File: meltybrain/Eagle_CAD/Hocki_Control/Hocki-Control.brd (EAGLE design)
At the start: 90 x 46 mm, 153 parts, among them J1 SM03B-SRSS-TB(LF)(SN), J2 SM04B-SRSS-TB(LF)(SN), J3 SM02B-SRSS-TB(LF)(SN), J4 SM04B-SRSS-TB(LF)(SN), J5 SM03B-SRSS-TB(LF)(SN), J6 SM03B-SRSS-TB(LF)(SN), U1 AP63200, U10 LMH6612MAX/NOPB, U11 TLV3502AIDCNR, U12 LMH6612MAX/NOPB, U13 TMP235A4DCKR, U14 ADXL375, U15 NL27WZ32USG, U16 ADXL375, U17 ADXL375, U18 NL27WZ32USG, U19 ADXL375, U2 TEENSY_4.1, U20 LMV358, U21 LMV358, U22 HMC1052L-TR, U23 LMV358, U24 IRF7509, U3 AP2210K-5.0TRG1, U4 AP2210K-3.3TRG1, U5 HEF4104BT,653, U6 LDL212PU50R, U7 LMH6612MAX/NOPB, U8 LMH6612MAX/NOPB, U9 TMUX1219DCKR

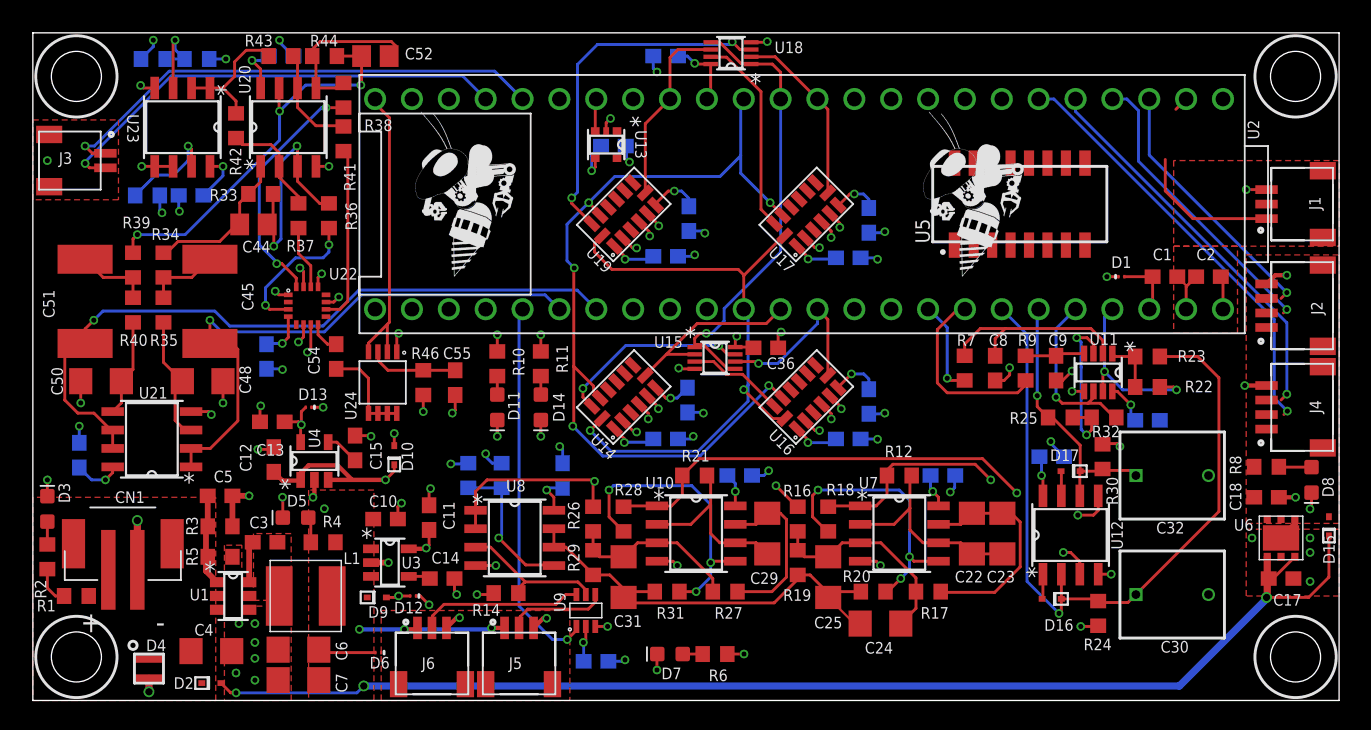
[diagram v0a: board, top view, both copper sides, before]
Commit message: fixed magnetometer issues
using instrumentation amplifier without filtering...fixes positive feedback as well
added ferrite bead
replaced remaining lmv358 to condense component list
TODO: esc connections
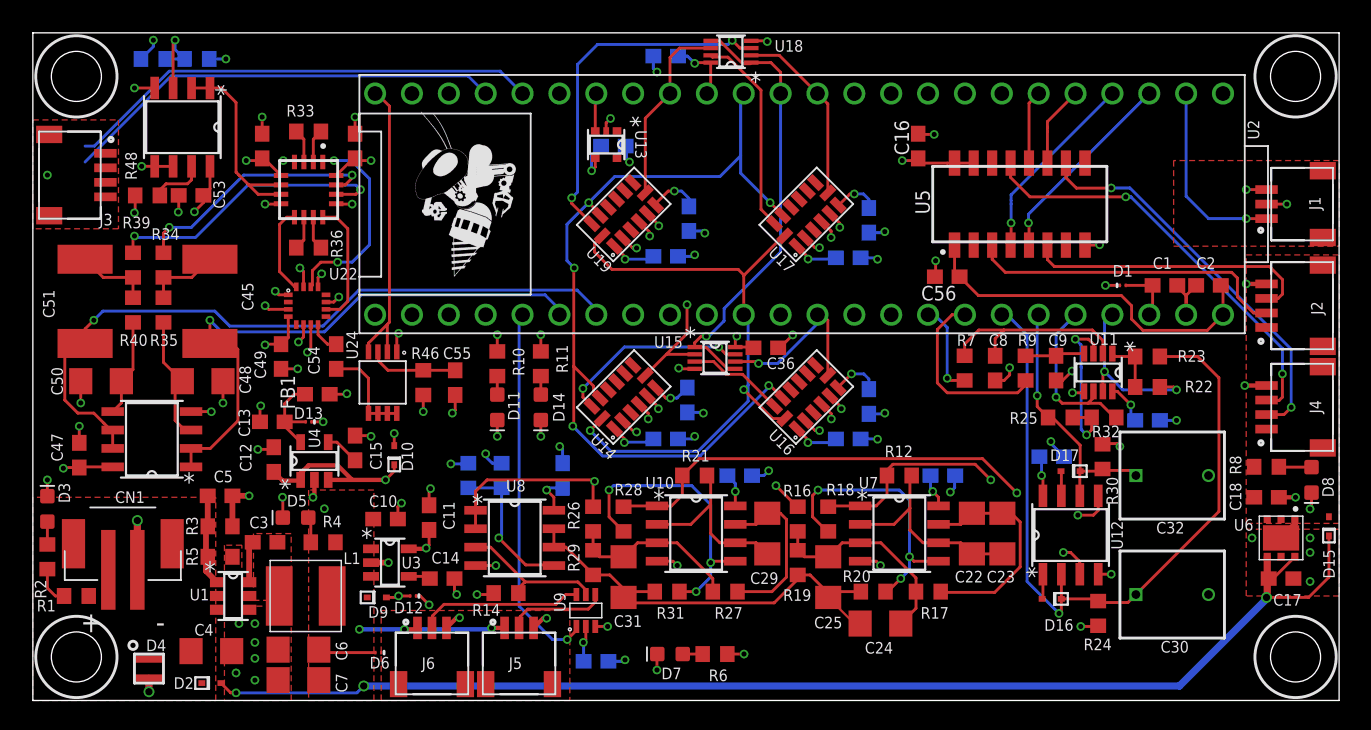
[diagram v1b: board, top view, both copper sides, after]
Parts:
- removed C52: 1000pF, rcl:C0805
- removed R37, R38, R41: 4.99k, rcl:R0603
- removed R42, R43, R44: 499k, rcl:R0603
- removed U$1: (no value), RoboJackets-Aesthetics:ROBOBUZZ_0.6X
- added C16, C56: 0.1uF, rcl:C0603
- added FB1: MPZ1608R391ATD25, Hocki_Library:0603
- C44: value 1000pF -> 0.1uF; device rcl:C0805 -> rcl:C0603
- CN1: value (none) -> JST_2PIN
- J3: value SM02B-SRSS-TB(LF)(SN) -> SM04B-SRSS-TB(LF)(SN); device Hocki_Library:SM02B-SRSS-TB(LF)(SN) -> Hocki_Library:SM04B-SRSS-TB(LF)(SN)
- R33: value 499k -> 49.9
- R36: value 4.99k -> 49.9
- U20: value LMV358 -> AD8426ACPZ-WP; device Hocki_Library:8-SOIC -> Hocki_Library:16LFCSP
- U21, U23: value LMV358 -> LMH6612MAX/NOPB
- moved C46 8.03 mm to (-29.8, 11.0), flipped to the top, turned to 90 degrees
- moved C44 5.43 mm to (-36.2, 11.0), turned to 90 degrees
- moved R33 5.42 mm to (-33.0, 12.0), turned to 180 degrees
- moved U20 4.52 mm to (-33.0, 8.00), turned to 270 degrees
- moved R36 2.61 mm to (-33.0, 4.00), turned to 180 degrees
- moved C49 1.00 mm to (-34.9, -3.50), flipped to the top
- moved D13 1.00 mm to (-33.0, -8.00)
- moved J3 1.00 mm to (-47.0, 9.00)
- moved D1 0.61 mm to (23.1, 1.40)
- moved C1 0.60 mm to (26.0, 1.40)
- moved C2 0.60 mm to (29.0, 1.40)
- moved U18 0.10 mm to (-3.90, 17.5)
- flipped C47 to the top
- flipped C53 to the top, turned to 180 degrees
- flipped R48 to the top
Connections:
- removed net MAG_OUTPUTA: C44.2, R33.1, R34.2, U20.1
- removed net MAG_OUTPUTB: C52.2, R39.2, R44.1, U20.7
- removed net OUT+(A): R36.2, U22.3
- removed net OUT+(B): R38.2, U22.16
- removed net OUT-(A): R37.2, U22.14
- removed net OUT-(B): R41.2, U22.10
- new net N$28: C13.1, D13.C2, FB1.1, U4.5
- new net N$31: U20.4, U22.3
- new net N$32: U20.1, U22.14
- new net N$33: U20.9, U22.16
- new net N$38: R33.1, U20.2
- new net N$39: R36.2, U20.10
- new net N$40: R36.1, U20.11
- net +3V3: now also C44.1, FB1.2, U20.16, U20.5; no longer C13.1, D13.C2, U20.8, U4.5
- net +5V: no longer U5.1
- net 3.3V: now also C16.1
- net 5V: now also C56.1, U5.1
- net ESC_L: no longer J3.1
- net ESC_R: no longer J3.2
- net GND: now also C16.2, C44.2, C56.2, U20.13, U20.8; no longer U20.4
- net LED_CLK2: now also U2.3; no longer U2.4
- net LED_DATA2: now also U2.4; no longer U2.3
- net N$34: now also U20.12, U22.10; no longer R41.1, R43.1, U20.6
- net N$35: now also R39.2, U20.14; no longer C52.1, R38.1, R44.2, U20.5
- net N$36: now also R34.2, U20.15; no longer R37.1, R42.1, U20.2
- net N$37: no longer C44.1, R36.1
- net VREF/2: now also U20.6, U20.7; no longer R42.2, R43.2
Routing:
- net B_LED_DATA2: track 0.00 -> 29.2 mm, vias 0 -> 2
- net MAG_OUTPUTB: track 27.5 -> 0.00 mm, vias 3 -> 0
- net B_LED_CLK2: track 0.00 -> 27.3 mm, vias 0 -> 2
- net LED_CLK2: track 29.6 -> 5.60 mm, vias 1 -> 0
- net 5V: track 30.9 -> 53.6 mm
- net 3.3V: track 47.1 -> 69.4 mm, vias 14 -> 16
- net B_LED_CLK1: track 0.00 -> 22.2 mm
- net LED_DATA2: track 26.9 -> 5.07 mm, vias 1 -> 0
- net B_LED_DATA1: track 0.00 -> 20.0 mm
- net OUT+(B): track 16.9 -> 0.00 mm, vias 2 -> 0
- net N$37: track 16.8 -> 2.32 mm, vias 2 -> 0
- net N$32: track 0.00 -> 14.2 mm, vias 0 -> 2
- net N$31: track 0.00 -> 13.0 mm, vias 0 -> 2
- net OUT-(B): track 12.2 -> 0.00 mm
- net MAG_OUTPUTA: track 10.7 -> 0.00 mm
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- added copper zone on layer 1, net 3.3V
- removed copper zone on layer 1, net 5V

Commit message: finished esc connections...moved connector a bit as well
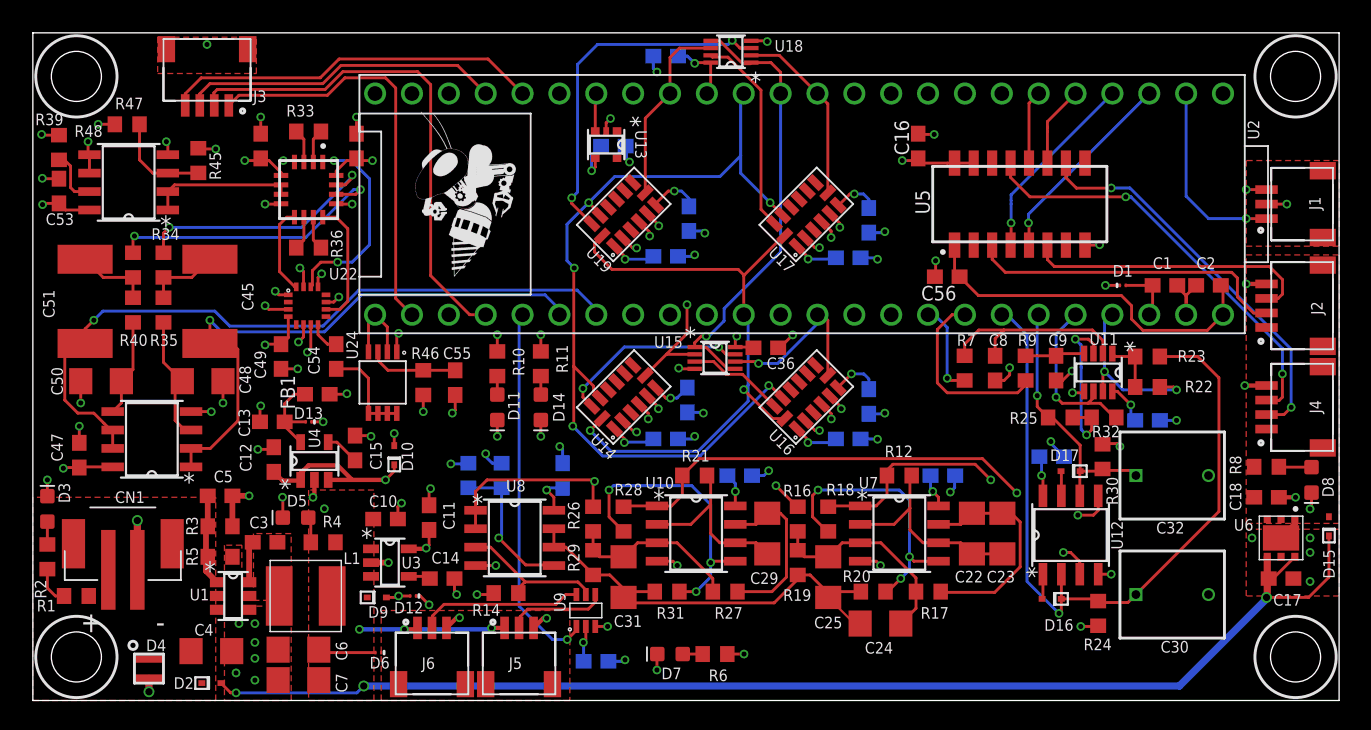
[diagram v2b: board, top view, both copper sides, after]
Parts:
- moved C53 9.10 mm to (-50.2, 7.90), turned to 90 degrees
- moved J3 8.49 mm to (-40.0, 13.8), turned to 180 degrees
- moved R45 7.00 mm to (-40.6, 10.0), flipped to the top, turned to 270 degrees
- moved R48 6.94 mm to (-50.2, 10.9), turned to 90 degrees
- moved U23 5.30 mm to (-45.4, 8.50), turned to 180 degrees
- moved R47 4.85 mm to (-45.5, 12.5), flipped to the top, turned to 180 degrees
- moved C46 0.10 mm to (-29.7, 11.0)
- moved C44 0.10 mm to (-36.3, 11.0)
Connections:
- new net ESC_TEL_L: J3.4, U2.28
- new net ESC_TEL_R: J3.1, U2.34
- net ESC_L: now also J3.3, U2.29; no longer U2.28
- net ESC_R: now also J3.2, U2.36; no longer U2.29
- net S/R: now also U2.33; no longer U2.32
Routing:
- net ESC_TEL_R: track 0.00 -> 28.7 mm
- net ESC_TEL_L: track 0.00 -> 26.0 mm
- net S/R: track 20.8 -> 5.66 mm
- net ESC_L: track 32.9 -> 22.1 mm
- net VREF/2: track 14.2 -> 9.91 mm
- net ESC_R: track 30.6 -> 34.9 mm
- net GND: track 124.7 -> 123.8 mm
- net N$23: track 6.22 -> 6.89 mm, vias 1 -> 0

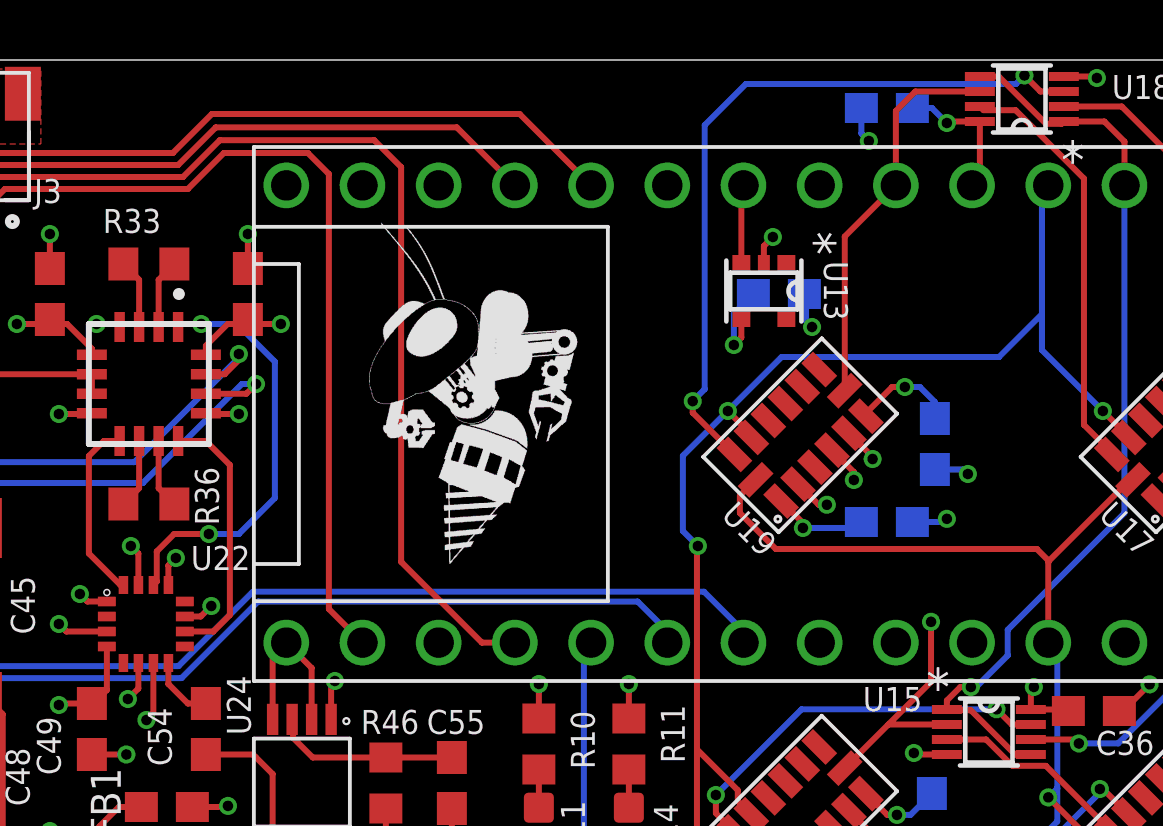
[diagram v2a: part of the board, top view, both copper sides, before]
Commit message: pin change on esc_r
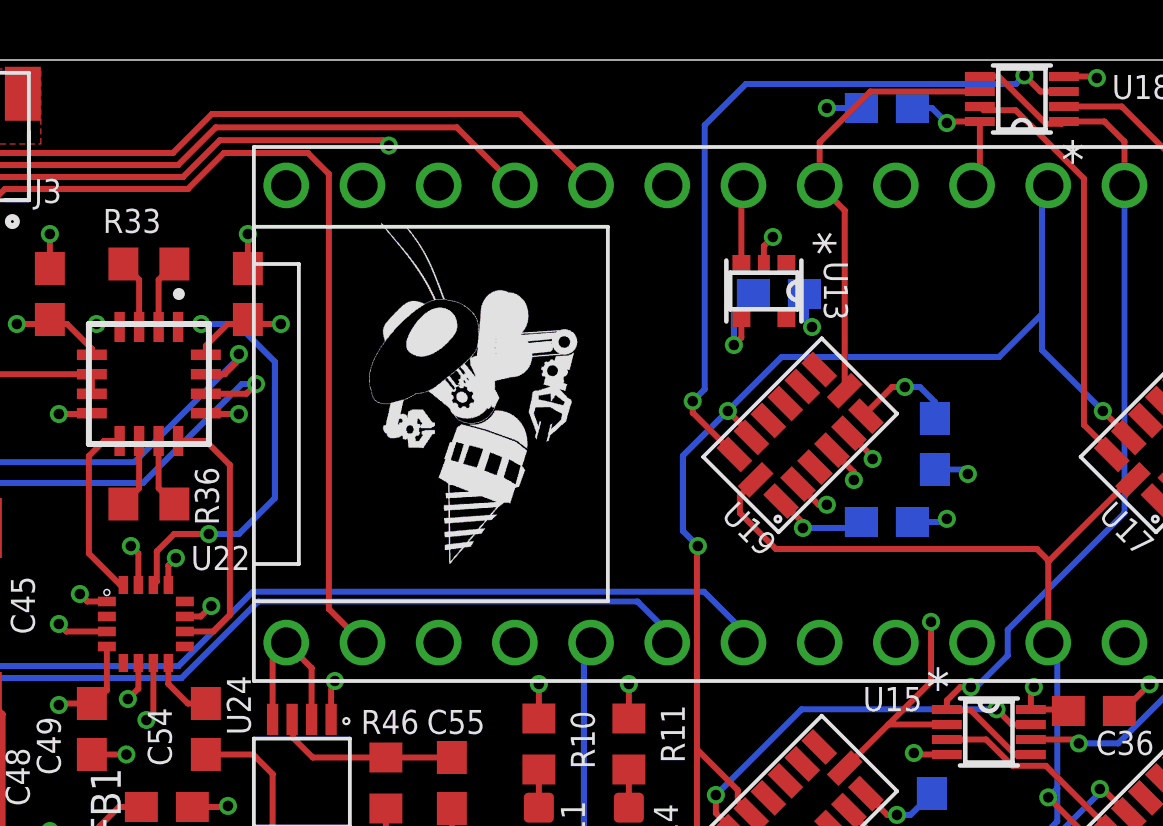
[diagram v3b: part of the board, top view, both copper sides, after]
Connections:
- net CS4: now also U2.25; no longer U2.24
- net ESC_R: now also U2.24; no longer U2.36
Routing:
- net CS4: track 13.1 -> 14.7 mm
- net ESC_R: track 34.9 -> 33.5 mm, vias 0 -> 1
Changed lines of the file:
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@@
 </element>
 <element name="C39" library="rcl" library_urn="urn:adsk.eagle:library:334" package="C0603" package3d_urn="urn:adsk.eagle:package:23616/2" value="0.1uF" x="-8.4" y="17.2" smashed="yes" rot="MR0">
-<attribute name="NAME" x="-10.165" y="16.835" size="0.8" layer="26" font="vector" ratio="15" rot="MR0"/>
+<attribute name="NAME" x="-9.965" y="16.035" size="0.8" layer="26" font="vector" ratio="15" rot="MR0"/>
 <attribute name="POPULARITY" value="37" x="-8.4" y="17.2" size="1.778" layer="28" rot="MR0" display="off"/>
 <attribute name="SPICEPREFIX" value="C" x="-8.4" y="17.2" size="1.778" layer="28" rot="MR0" display="off"/>
@@
 <wire x1="-11.094" y1="10.1" x2="-10.894" y2="9.9" width="0.2" layer="16"/>
 <via x="-10.894" y="9.9" extent="1-16" drill="0.35"/>
-<wire x1="-9.25" y1="17.2" x2="-9.25" y2="16.35" width="0.2" layer="16"/>
-<wire x1="-9.25" y1="16.35" x2="-9" y2="16.1" width="0.2" layer="16"/>
-<via x="-9" y="16.1" extent="1-16" drill="0.35"/>
+<wire x1="-9.25" y1="17.2" x2="-10.4" y2="17.2" width="0.2" layer="16"/>
+<via x="-10.4" y="17.2" extent="1-16" drill="0.35"/>
 <contactref element="U5" pad="8"/>
 <wire x1="20.495" y1="4.175" x2="21.475" y2="4.175" width="0.2" layer="1"/>
@@
 <contactref element="U18" pad="6"/>
 <contactref element="U19" pad="7"/>
-<contactref element="U2" pad="24"/>
-<wire x1="-8.1" y1="14.62" x2="-8.1" y2="17.1" width="0.2" layer="1"/>
-<wire x1="-8.1" y1="17.1" x2="-7.45" y2="17.75" width="0.2" layer="1"/>
-<wire x1="-7.45" y1="17.75" x2="-5.3" y2="17.75" width="0.2" layer="1"/>
-<wire x1="-8.1" y1="14.62" x2="-9.805075" y2="12.914925" width="0.2" layer="1"/>
-<wire x1="-9.805075" y1="12.914925" x2="-9.805075" y2="7.774921875" width="0.2" layer="1"/>
+<wire x1="-8.95" y1="17.75" x2="-5.3" y2="17.75" width="0.2" layer="1"/>
+<contactref element="U2" pad="25"/>
+<wire x1="-9.805075" y1="13.785075" x2="-10.64" y2="14.62" width="0.2" layer="1"/>
+<wire x1="-9.805075" y1="7.774921875" x2="-9.805075" y2="13.785075" width="0.2" layer="1"/>
+<wire x1="-8.95" y1="17.75" x2="-10.64" y2="16.06" width="0.2" layer="1"/>
+<wire x1="-10.64" y1="14.62" x2="-10.64" y2="16.06" width="0.2" layer="1"/>
 </signal>
 <signal name="CS2">
@@
 </signal>
 <signal name="ESC_R">
-<contactref element="U2" pad="36"/>
 <contactref element="J3" pad="2"/>
-<wire x1="-20.8" y1="-0.62" x2="-21.9" y2="-0.62" width="0.2" layer="1"/>
-<wire x1="-21.9" y1="-0.62" x2="-24.591" y2="2.071" width="0.2" layer="1"/>
-<wire x1="-24.591" y1="2.071" x2="-24.591" y2="15.2296625" width="0.2" layer="1"/>
-<wire x1="-30.63545" y1="16.127" x2="-31.86245" y2="14.9" width="0.2" layer="1"/>
-<wire x1="-24.591" y1="15.2296625" x2="-25.4883375" y2="16.127" width="0.2" layer="1"/>
-<wire x1="-25.4883375" y1="16.127" x2="-30.63545" y2="16.127" width="0.2" layer="1"/>
+<wire x1="-31.86245" y1="14.9" x2="-30.63545" y2="16.127" width="0.2" layer="1"/>
 <wire x1="-39.5" y1="13.8" x2="-39.527" y2="13.827" width="0.2" layer="1"/>
 <wire x1="-39.527" y1="14.669025" x2="-39.527" y2="13.827" width="0.2" layer="1"/>
 <wire x1="-39.296025" y1="14.9" x2="-39.527" y2="14.669025" width="0.2" layer="1"/>
 <wire x1="-31.86245" y1="14.9" x2="-39.296025" y2="14.9" width="0.2" layer="1"/>
+<contactref element="U2" pad="24"/>
+<wire x1="-25.1782" y1="16.127" x2="-25" y2="15.9488" width="0.2" layer="1"/>
+<via x="-25" y="15.9488" extent="1-16" drill="0.35"/>
+<wire x1="-30.63545" y1="16.127" x2="-25.1782" y2="16.127" width="0.2" layer="1"/>
+<wire x1="-25" y1="15.9488" x2="-9.4288" y2="15.9488" width="0.2" layer="15"/>
+<wire x1="-9.4288" y1="15.9488" x2="-8.1" y2="14.62" width="0.2" layer="15"/>
 </signal>
 <signal name="N$14">
